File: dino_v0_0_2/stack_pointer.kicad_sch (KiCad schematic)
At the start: 15 parts, among them U63 74LS169, U64 74LS169, U65 74LS169, U66 74LS169, U67 74LS245, U68 74LS245, U69 74LS08

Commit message: feat(kicad): footprints, power sheet, global labels, PCB draft
Every symbol gets a stock THT footprint (plain DIP, no sockets, so the
3D render shows ICs). New Power sheet: 24-pin ATX header for a picoPSU,
rails +5V/+3.3V/+12V/-12V/GND only; no -5V exists on any ATX unit since
2003, none drawn. PS_ON# on a 2-pin header.

Cross-sheet labels become global labels. KiCad joined nothing between
sheets before: 122 base names were split per sheet, ERC saw 90 undriven
inputs whose driver sat one sheet away, and the PCB ratsnest stopped at
every sheet boundary. Proof: KiCad's netlist after equals a name-join of
its netlist before plus the 15 CW alias pairs, pin for pin.

kicad_contracts took a node's sheet from the net name's /Sheet/ prefix;
global nets have none, so it emitted an empty contracts doc. Sheet now
comes from the component's own path; the doc regenerates with zero diff.

ERC 477 -> 2. Real fixes: ROM I/O pins input -> tri_state, '382 GND pin
power_out -> power_in, four orphan symbols rehomed to project lib `dino`,
one stub wire. 133 by-design warnings excluded by uuid ('245 readback on
counter Q, alias stubs, probe-point labels); the two left are bus
signals the peripheral bus sheet will consume.

PCB draft: 198 footprints placed per sheet, all pads netted, no tracks.

Co-Authored-By: Claude Fable 5.1 <noreply@anthropic.com>
Claude-Session: https://claude.ai/code/session_018irreFHb1xEykW5kCD26ow
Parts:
- C68, C69, C70, C71, C72, C73, C74: footprint (none) -> Capacitor_THT:C_Disc_D5.0mm_W2.5mm_P2.50mm
- R2: footprint (none) -> Resistor_THT:R_Axial_DIN0207_L6.3mm_D2.5mm_P10.16mm_Horizontal
- U63, U64, U65, U66: footprint (none) -> Package_DIP:DIP-16_W7.62mm
- U67, U68: footprint (none) -> Package_DIP:DIP-20_W7.62mm
- U69: footprint (none) -> Package_DIP:DIP-14_W7.62mm

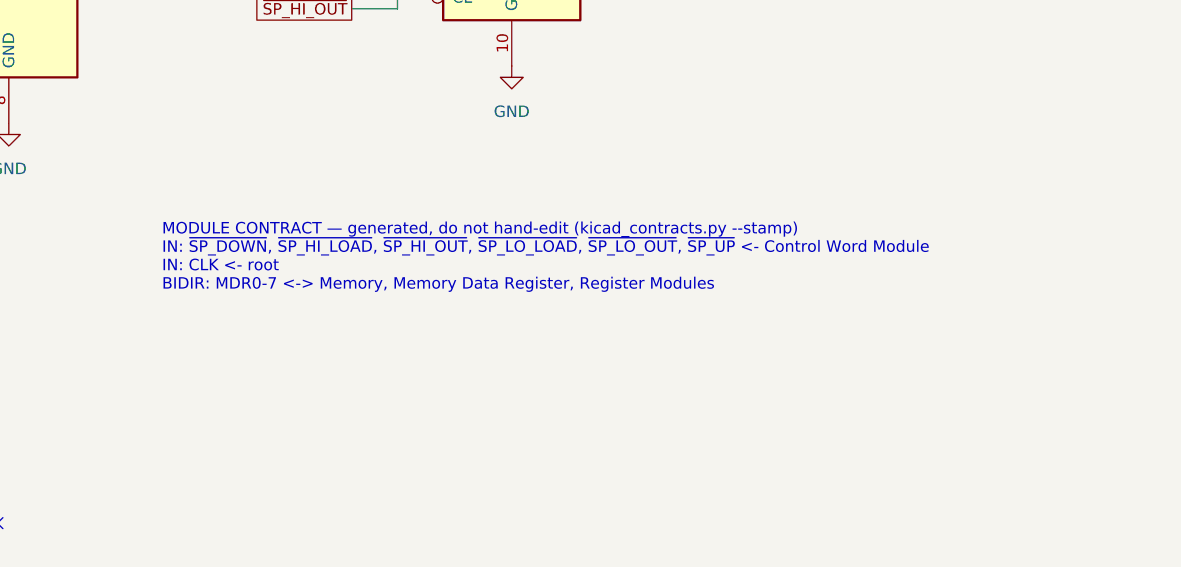
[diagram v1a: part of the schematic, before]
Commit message: feat(int): draw the interrupt block; sheet cleanup pass
New sheet dino_v0_0_2/interrupt.kicad_sch (page 15): U80-U87, R28 4.7k
pull-up on ~{IRQ}, R29 100R on the block's CLK branch, C83-C90. Every
pin per PHASE_INT SECTION 3, checked against the plan with kicad_netlist
and kicad-cli (146 pins, 0 mismatches).

Old sheets (SECTION 3.2): U28.4 lifted off GND to INJECT; U61.3 to
END_OR_ACCEPT; U36.1 to PC_UP_GATED; U49 D0-3 cut from U48 Za-Zd and
routed through U87 as FLAG_NEXT0-3 / FLAG_D0-3; FLAG_C/Z/V/N and the
five decoder outputs made global. dino_serial: U104 74LS05, INTR ->
~{IRQ}, C4.

Placement pass on every sheet: bus entries and global labels no longer
share wires; M, CW, T, IRB and SA buses kept as labelled keys. Nets
diffed against HEAD per sheet: only the intended changes and a rotated
C29. Project ERC: 0 errors. MODULE CONTRACT stamps regenerated.

Co-Authored-By: Claude Fable 5.1 <noreply@anthropic.com>
Claude-Session: https://claude.ai/code/session_01JGxSS4MVUcaZdKZGtKroSg
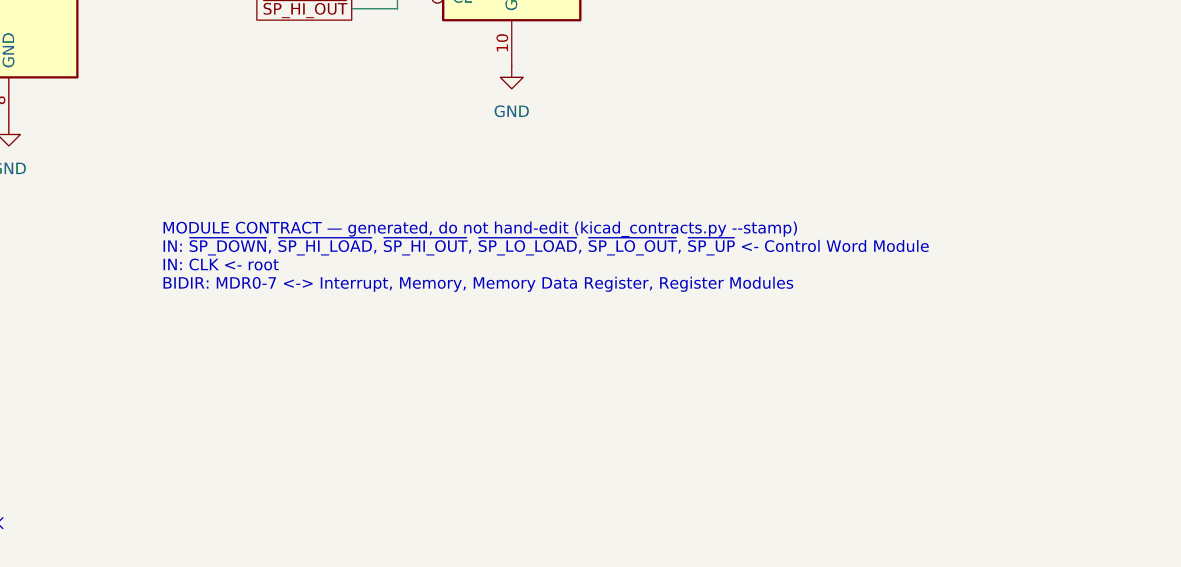
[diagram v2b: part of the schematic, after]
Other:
- note added: "MODULE CONTRACT — generated, do not hand-edit (kicad_contracts.py --stamp) IN: ~{SP_DOWN}, ~{SP_HI_LOAD}, ~{SP_HI_OUT}, ~{SP_LO_LOAD}, ~{SP_LO_OUT}, ~{SP_UP} <- Control Word Module IN: CLK <- root BIDIR: MDR0-7 <-> Interrupt, Memory, Memory Data Register, Register Modules"
- note removed: "MODULE CONTRACT — generated, do not hand-edit (kicad_contracts.py --stamp) IN: ~{SP_DOWN}, ~{SP_HI_LOAD}, ~{SP_HI_OUT}, ~{SP_LO_LOAD}, ~{SP_LO_OUT}, ~{SP_UP} <- Control Word Module IN: CLK <- root BIDIR: MDR0-7 <-> Memory, Memory Data Register, Register Modules"
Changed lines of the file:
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@@
 		(comment 4 "A Turing-Complete 8-bit \"Computer\"")
 	)
-	(text "MODULE CONTRACT — generated, do not hand-edit (kicad_contracts.py --stamp)\nIN: ~{SP_DOWN}, ~{SP_HI_LOAD}, ~{SP_HI_OUT}, ~{SP_LO_LOAD}, ~{SP_LO_OUT}, ~{SP_UP} <- Control Word Module\nIN: CLK <- root\nBIDIR: MDR0-7 <-> Memory, Memory Data Register, Register Modules"
+	(text "MODULE CONTRACT — generated, do not hand-edit (kicad_contracts.py --stamp)\nIN: ~{SP_DOWN}, ~{SP_HI_LOAD}, ~{SP_HI_OUT}, ~{SP_LO_LOAD}, ~{SP_LO_OUT}, ~{SP_UP} <- Control Word Module\nIN: CLK <- root\nBIDIR: MDR0-7 <-> Interrupt, Memory, Memory Data Register, Register Modules"
 		(exclude_from_sim no)
 		(at 177.038 162.306 0)
